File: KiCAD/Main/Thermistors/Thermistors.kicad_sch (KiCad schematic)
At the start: 6 parts, among them J3 Conn_01x02_Socket, J6 Conn_01x02_Socket, J7 Conn_01x02_Socket, J8 Conn_01x02_Socket, U5 LT3092xST, U6 ADG5234BRUZ

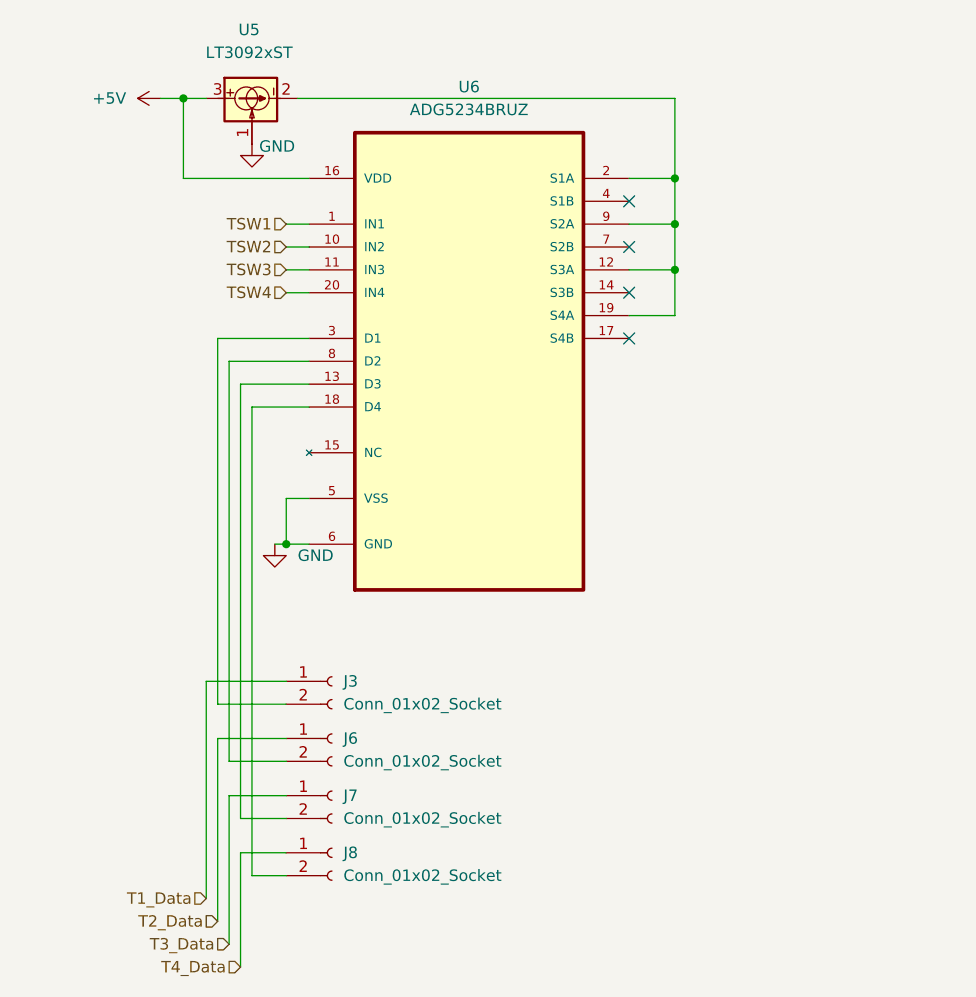
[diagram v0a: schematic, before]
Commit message: Remove thermocouples due to complexity and focus switch
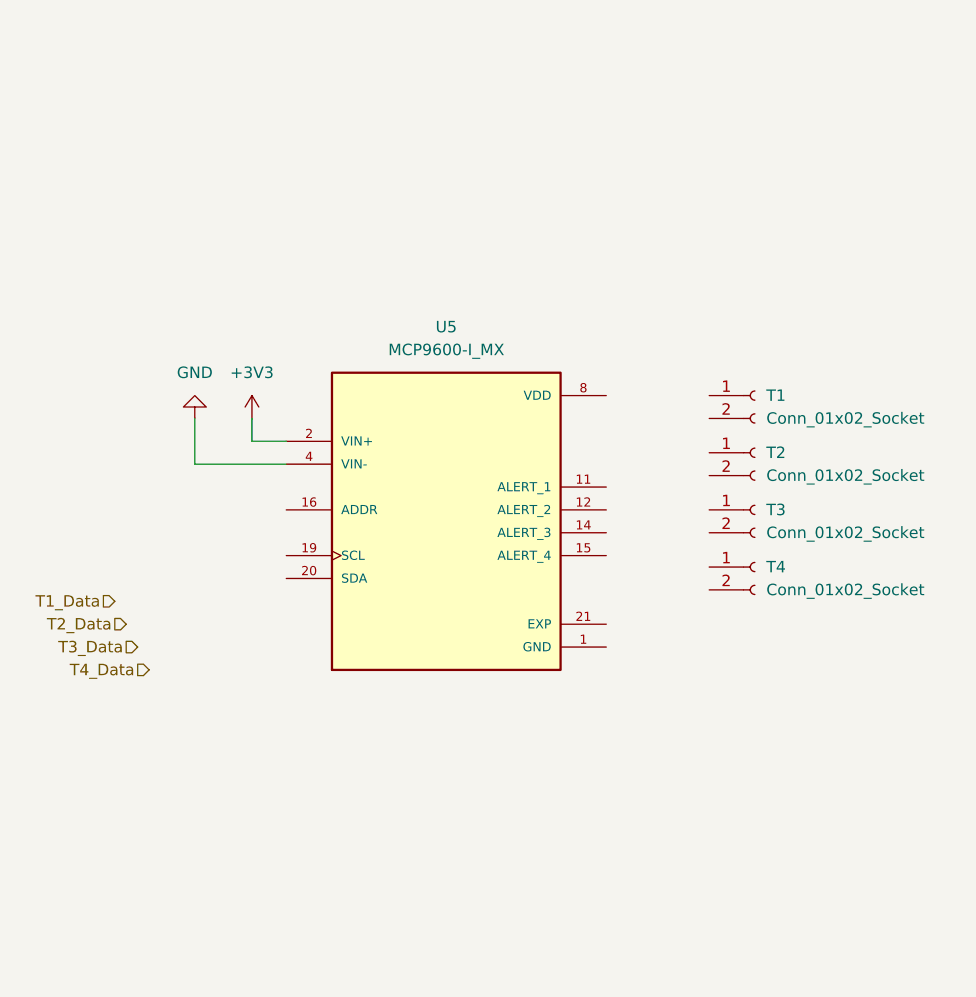
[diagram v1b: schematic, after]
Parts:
- removed U5: LT3092xST, Package_TO_SOT_SMD:SOT-223-3_TabPin2, symbol Reference_Current:LT3092xST
- removed U6: ADG5234BRUZ, ADG5234BRUZ:SOP65P640X120-20N, symbol ADG5234BRUZ:ADG5234BRUZ
- added U5: MCP9600-I_MX, MCP9600-I_MX:QFN65P500X500X100-21N, symbol MCP9600-I_MX:MCP9600-I_MX
- renumbered J3 to T1, J6 to T2, J7 to T3, J8 to T4
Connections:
- net GND: now also U5.1 (GND), U5.10 (GND), U5.13 (GND), U5.17 (GND), U5.18 (GND), U5.3 (GND), U5.4 (VIN-), U5.5 (GND), U5.6 (GND), U5.7 (GND), U5.9 (GND)
- net T1_Data: no longer T1.1 (Pin_1)
- net T2_Data: no longer T2.1 (Pin_1)
- net T3_Data: no longer T3.1 (Pin_1)
- net T4_Data: no longer T4.1 (Pin_1)
- new net +3V3: U5.2 (VIN+)
- new net EXP: U5.21 (EXP), U5.22 (EXP), U5.23 (EXP), U5.24 (EXP), U5.25 (EXP), U5.26 (EXP), U5.27 (EXP), U5.28 (EXP), U5.29 (EXP), U5.30 (EXP)
- no-connect marks 4 -> 0
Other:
- moved on the sheet: T1, T2, T3, T4
